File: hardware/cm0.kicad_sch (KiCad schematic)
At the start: 0 parts

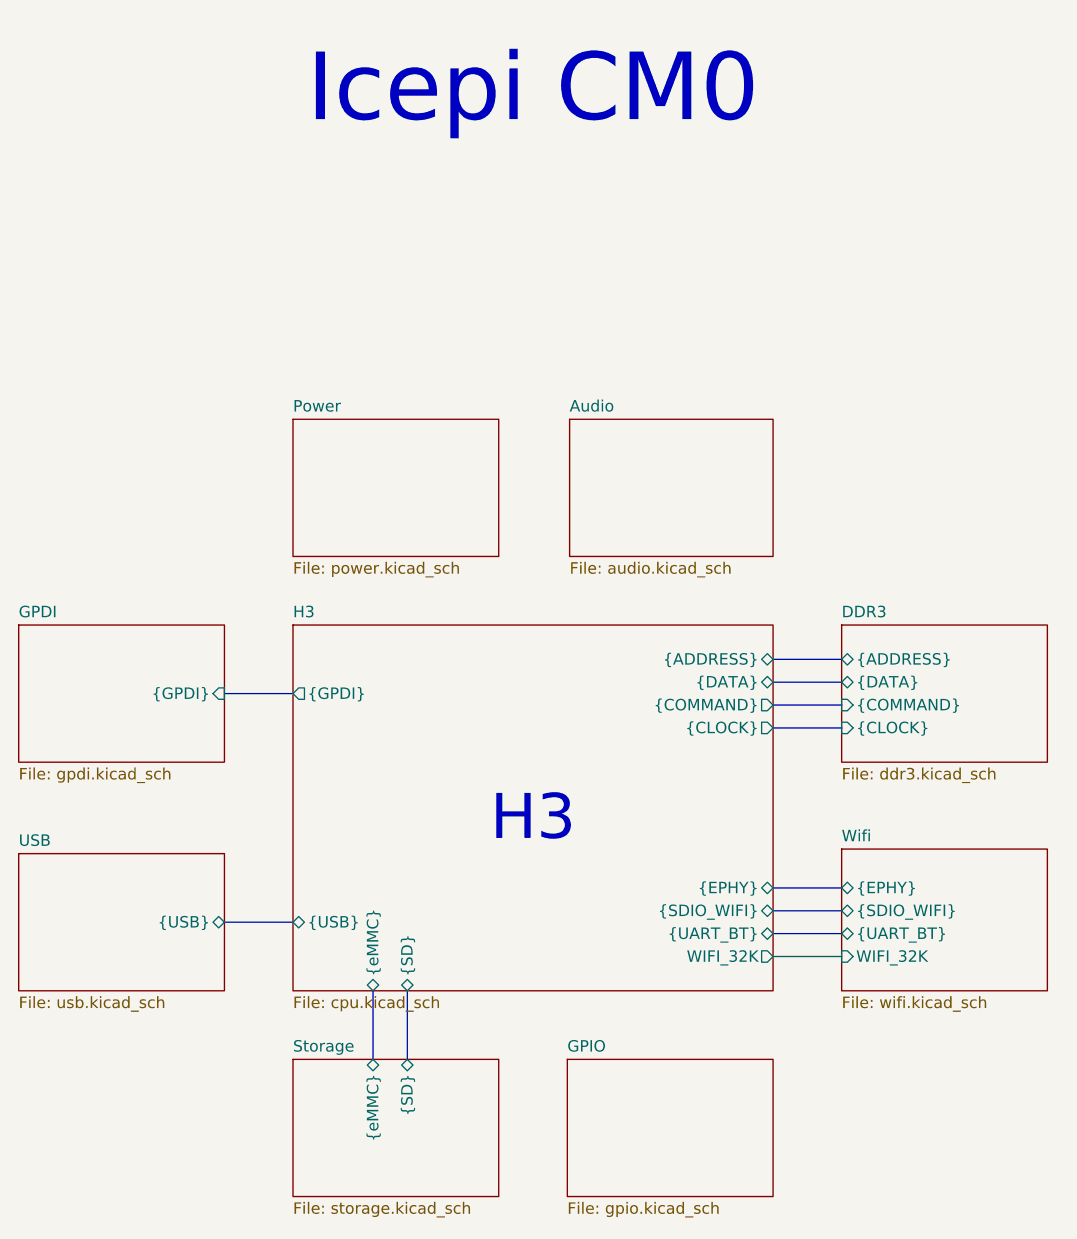
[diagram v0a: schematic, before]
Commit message: Drew most of DC DC converters
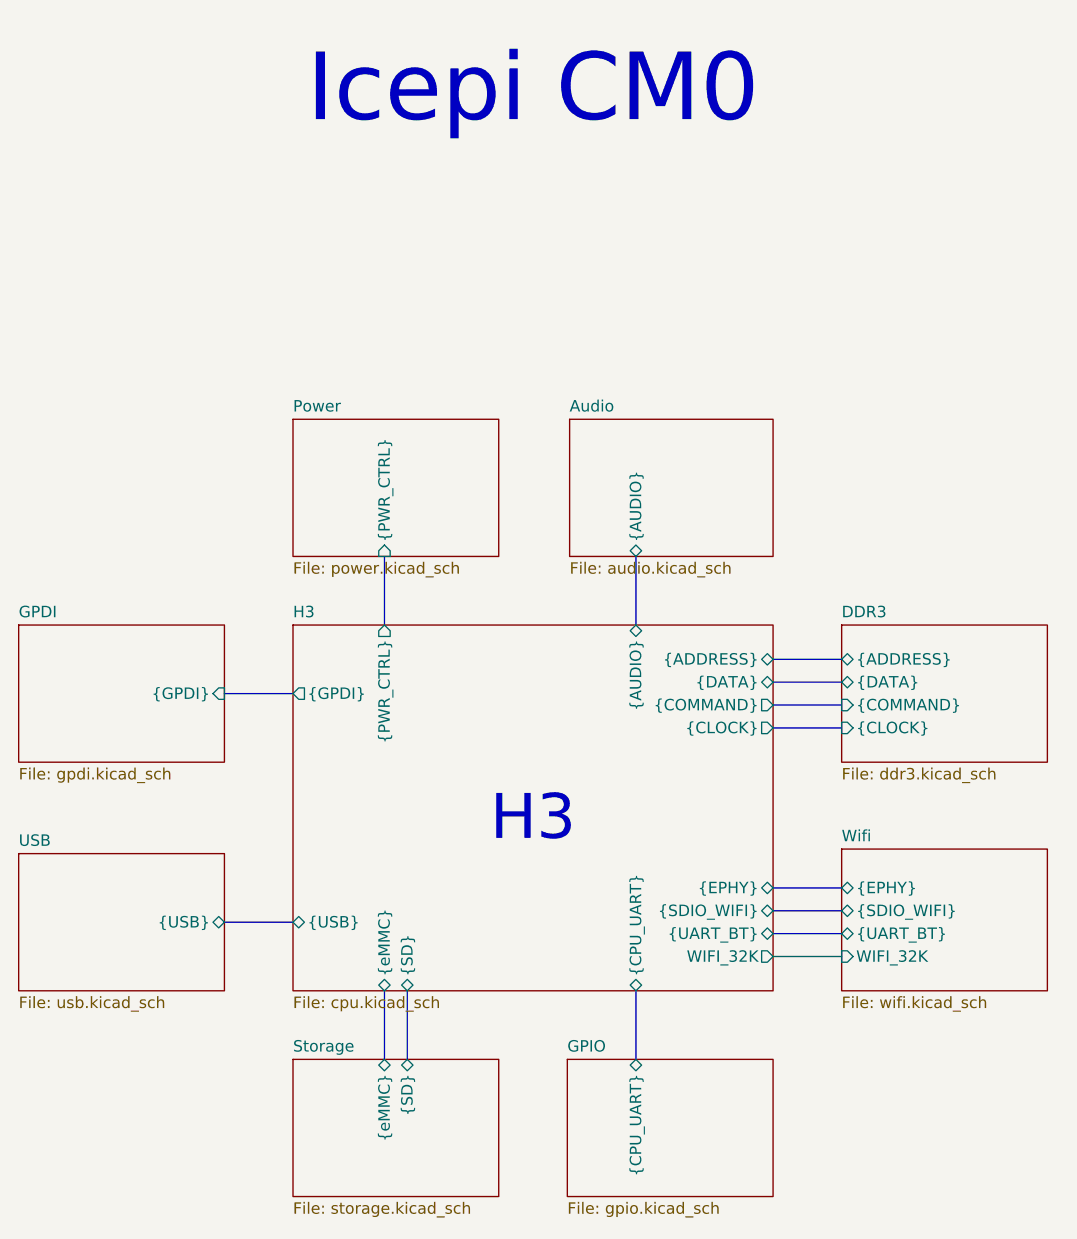
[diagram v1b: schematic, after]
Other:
- sheet Audio ports: added {AUDIO}; removed none
- sheet GPIO ports: added {CPU_UART}; removed none
- sheet H3 ports: added {AUDIO}, {CPU_UART}, {PWR_CTRL}; removed none
- sheet Power ports: added {PWR_CTRL}; removed none
